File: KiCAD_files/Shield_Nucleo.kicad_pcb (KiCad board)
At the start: 4 copper layers, 90 x 100 mm, 62 parts, among them J1 Shield_nucleo_stage_outline, J2 RJ45_LED_Shielded, J3 RJ45_LED_Shielded, J4 Conn_01x02_Male, J5 Conn_01x04_Male, U1 NUCLEO-F401RE, U2 AT25xxx, U3 TCAN334GDR

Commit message: WIP: nearly finished composant placement
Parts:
- removed J1: Shield_nucleo_stage_outline, Footprints:Shield_nucleo_outline
- added C10: 100nF, Capacitor_SMD:C_0805_2012Metric, F.Cu at (61.5, 84.9)
- added C11: 100nF, Capacitor_SMD:C_0805_2012Metric, F.Cu at (119.4, 51.1)
- added C12: 1µF, Capacitor_SMD:C_0805_2012Metric, F.Cu at (94.9, 82.4)
- added C13: 100nF, Capacitor_SMD:C_0805_2012Metric, F.Cu at (118.3, 44.4)
- added C14: 10nF, Capacitor_SMD:C_0805_2012Metric, F.Cu at (91.1, 80.5)
- added C17: 33pF, Capacitor_SMD:C_0805_2012Metric, F.Cu at (122.5, 57.4)
- added C18: 33pF, Capacitor_SMD:C_0805_2012Metric, F.Cu at (122.8, 50.2)
- added C20: 100nF, Capacitor_SMD:C_0805_2012Metric, F.Cu at (121.2, 47.4)
- added C21: 100nF, Capacitor_SMD:C_0805_2012Metric, F.Cu at (106.2, 53.8)
- added C22: 100nF, Capacitor_SMD:C_0805_2012Metric, F.Cu at (108.2, 47.2)
- added C23: 1uF, Capacitor_SMD:C_0805_2012Metric, F.Cu at (104.4, 53.8)
- added C24: 10uF, Capacitor_SMD:C_1210_3225Metric, F.Cu at (104.4, 46.5)
- added C25: 100nF, Capacitor_SMD:C_0805_2012Metric, F.Cu at (71.3, 50.4)
- added C26: 100nF, Capacitor_SMD:C_0805_2012Metric, F.Cu at (70.3, 43.6)
- added C27: 33pF, Capacitor_SMD:C_0805_2012Metric, F.Cu at (74.6, 55.8)
- added C28: 33pF, Capacitor_SMD:C_0805_2012Metric, F.Cu at (74.6, 50.4)
- added C3: 12pF, Capacitor_SMD:C_0805_2012Metric, F.Cu at (70.3, 80.3)
- added C30: 100nF, Capacitor_SMD:C_0805_2012Metric, F.Cu at (73.1, 46.7)
- added C31: 100nF, Capacitor_SMD:C_0805_2012Metric, F.Cu at (59.1, 52.8)
- added C32: 100nF, Capacitor_SMD:C_0805_2012Metric, F.Cu at (59.7, 46.6)
- added C33: 1uF, Capacitor_SMD:C_0805_2012Metric, F.Cu at (57.3, 52.8)
- added C34: 10uF, Capacitor_SMD:C_1210_3225Metric, F.Cu at (55.7, 46.1)
- added C4: 12pF, Capacitor_SMD:C_0805_2012Metric, F.Cu at (74.8, 85.2)
- added C5: 100nF, Capacitor_SMD:C_0805_2012Metric, F.Cu at (60.3, 80.3)
- added C6: 4,7uF, Capacitor_SMD:C_0805_2012Metric, F.Cu at (-3.77, 84.7)
- added C7: 100nF, Capacitor_SMD:C_0805_2012Metric, F.Cu at (73.2, 71.6)
- added C8: 100nF, Capacitor_SMD:C_0805_2012Metric, F.Cu at (86.0, 67.2)
- added C9: 100nF, Capacitor_SMD:C_0805_2012Metric, F.Cu at (92.9, 78.6)
- added D10: STTH4R02U, Diode_SMD:D_SMB, F.Cu at (105.4, 59.2)
- added D11: STTH4R02U, Diode_SMD:D_SMB, F.Cu at (58.3, 58.1)
- added D3: 3.3V, Diode_SMD:D_SOD-123, F.Cu at (80.0, 94.4)
- added D4: 3.3V, Diode_SMD:D_SOD-123, F.Cu at (73.7, 99.1)
- added D5: 3.3V, Diode_SMD:D_SOD-123, F.Cu at (90.2, 94.4)
- added D6: 3.3V, Diode_SMD:D_SOD-123, F.Cu at (94.0, 99.1)
- added D7: 3.3V, Diode_SMD:D_SOD-123, F.Cu at (79.6, 104.1)
- added D8: 3.3V, Diode_SMD:D_SOD-123, F.Cu at (90.2, 105.4)
- added D9: 3.3V, Diode_SMD:D_SOD-123, F.Cu at (69.5, 105.4)
- added FB1: Ferrite_Bead_Small, Resistor_SMD:R_0805_2012Metric, F.Cu at (94.2, 77.3)
- added PS1: IA0505S, Converter_DCDC:Converter_DCDC_muRata_CRE1xxxxxx3C_THT, F.Cu at (105.5, 115.4)
- added PS2: IA0512S, Converter_DCDC:Converter_DCDC_muRata_CRE1xxxxxx3C_THT, F.Cu at (97.8, 115.4)
- added PS4: PQDE6W-Q110-S5-D, Footprints:PQDE6W-Q110-S5-D, F.Cu at (124.5, 113.2)
- added R14: 51, Resistor_SMD:R_0805_2012Metric, F.Cu at (122.6, 52.6)
- added R15: 20k, Resistor_SMD:R_0805_2012Metric, F.Cu at (119.4, 47.3)
- added R16: 2.2, Resistor_SMD:R_0805_2012Metric, F.Cu at (103.2, 63.0)
- added R17: 51, Resistor_SMD:R_0805_2012Metric, F.Cu at (74.6, 54.0)
- added R18: 51, Resistor_SMD:R_0805_2012Metric, F.Cu at (74.6, 52.2)
- added R19: 20k, Resistor_SMD:R_0805_2012Metric, F.Cu at (71.3, 46.7)
- added R20: 2.2, Resistor_SMD:R_0805_2012Metric, F.Cu at (60.7, 61.9)
- added R21: 51, Resistor_SMD:R_0805_2012Metric, F.Cu at (82.2, 111.8)
- added R22: 1k, Resistor_SMD:R_0805_2012Metric, F.Cu at (82.2, 119.4)
- added R23: 220, Resistor_SMD:R_0805_2012Metric, F.Cu at (75.8, 81.2)
- added TP16: TestPoint, TestPoint:TestPoint_Pad_D1.5mm, B.Cu at (134.7, 107.4)
- added TP31: TestPoint, TestPoint:TestPoint_Pad_D1.5mm, B.Cu at (50.0, 48.3)
- added TP34: TestPoint, TestPoint:TestPoint_Pad_D1.5mm, B.Cu at (94.2, 45.3)
- added TP35: TestPoint, TestPoint:TestPoint_Pad_D1.5mm, B.Cu at (94.2, 58.4)
- added TP36: TestPoint, TestPoint:TestPoint_Pad_D1.5mm, B.Cu at (94.2, 47.9)
- added TP37: TestPoint, TestPoint:TestPoint_Pad_D1.5mm, B.Cu at (83.8, 121.9)
- added TP38: TestPoint, TestPoint:TestPoint_Pad_D1.5mm, B.Cu at (81.1, 103.9)
- added TP39: TestPoint, TestPoint:TestPoint_Pad_D1.5mm, B.Cu at (89.3, 105.7)
- added TP40: TestPoint, TestPoint:TestPoint_Pad_D1.5mm, B.Cu at (79.4, 95.9)
- added TP41: TestPoint, TestPoint:TestPoint_Pad_D1.5mm, B.Cu at (89.7, 95.8)
- added TP42: TestPoint, TestPoint:TestPoint_Pad_D1.5mm, B.Cu at (92.2, 98.4)
- added TP43: TestPoint, TestPoint:TestPoint_Pad_D1.5mm, B.Cu at (50.0, 61.0)
- added TP44: TestPoint, TestPoint:TestPoint_Pad_D1.5mm, B.Cu at (94.2, 61.0)
- added TP45: TestPoint, TestPoint:TestPoint_Pad_D1.5mm, B.Cu at (81.3, 121.9)
- added U4: AP1117-33, Package_TO_SOT_SMD:SOT-223-3_TabPin2, F.Cu at (111.0, 76.2)
- added U5: UCC21222DR, Package_SO:SOIC-16_4.55x10.3mm_P1.27mm, F.Cu at (114.0, 50.2)
- added U6: UCC21222DR, Package_SO:SOIC-16_4.55x10.3mm_P1.27mm, F.Cu at (65.7, 49.6)
- added U7: SFH617A-2X009T, Package_DIP:SMDIP-4_W7.62mm, F.Cu at (85.8, 115.8)
- added Y1: NX3225SA-16.000000MHZ-T1, Crystal:Crystal_SMD_3225-4Pin_3.2x2.5mm, F.Cu at (72.4, 82.8)
- BT1, C1, C2, D1, D2, F1, F2, JP1, R1, R2, R4, R6, R8, U2, U3: moved to F.Cu
- R3, R5, R7: value 39k -> 20k; moved to F.Cu
- R9: value 39k -> 51; moved to F.Cu
- TP1, TP10, TP11, TP12, TP13, TP14, TP15, TP17, TP18, TP19, TP2, TP20, TP3, TP32, TP33, TP4, TP5, TP6, TP7, TP8, TP9: footprint TestPoint:TestPoint_THTPad_D2.0mm_Drill1.0mm -> TestPoint:TestPoint_Pad_D1.5mm
- TP21, TP22, TP23, TP24, TP25, TP26, TP27, TP28, TP29, TP30: footprint TestPoint:TestPoint_THTPad_D2.0mm_Drill1.0mm -> TestPoint:TestPoint_Pad_D1.5mm; moved to B.Cu
- U1: value NUCLEO-F401RE -> STM32G474RE; footprint Footprints:ST_NUCLEO-G474 -> Package_QFP:LQFP-64_10x10mm_P0.5mm
- moved J2 129.7 mm to (187.7, 27.4), turned to 180 degrees
- moved R11 129.5 mm to (192.8, 33.2), turned to 270 degrees
- moved R10 112.7 mm to (181.4, 33.1), turned to 270 degrees
- moved J3 104.5 mm to (167.6, 27.4), turned to 180 degrees
- moved C2 102.9 mm to (182.5, 46.0), turned to 90 degrees
- moved U3 101.4 mm to (187.1, 46.0)
- moved R13 101.2 mm to (172.7, 33.0), turned to 270 degrees
- moved JP1 100.6 mm to (192.2, 44.4), turned to 270 degrees
- moved R1 97.5 mm to (192.2, 47.1), turned to 270 degrees
- moved BT1 90.7 mm to (50.8, 111.9), turned to 90 degrees
- moved R12 88.8 mm to (161.3, 33.1), turned to 270 degrees
- moved J4 84.1 mm to (152.2, 109.6)
- moved F1 82.6 mm to (175.0, 46.2)
- moved J5 81.8 mm to (152.2, 115.4)
- moved TP22 80.2 mm to (134.7, 118.8), turned to 180 degrees
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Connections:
- R2 pad 1: Net-(J1-Pad9) -> /I1_low_mcu
- R2 pad 2: /I1_low -> /I1_low_op
- R3 pad 1: /I1_low -> /V1_low_mcu
- R3 pad 2: GNDD -> /V1_low_op
- R4 pad 1: Net-(J1-Pad10) -> /I1_low_mcu
- R4 pad 2: /I2_low -> /I2_low_op
- R5 pad 1: /I2_low -> /V2_low_mcu
- R5 pad 2: GNDD -> /V2_low_op
- R6 pad 1: Net-(J1-Pad11) -> /I_high_mcu
- R6 pad 2: /I_high -> /I_high_op
- R7 pad 1: /I_high -> /V_high_mcu
- R7 pad 2: GNDD -> /V_high_op
- R8 pad 1: Net-(J1-Pad12) -> /Temp
- R9 pad 1: /Temp -> /HRTIM1_CHA1
- R9 pad 2: GNDD -> Net-(C17-Pad2)
- TP21 pad 1: /V1_low_P -> /V1_low_op
- TP22 pad 1: /V1_low_N -> GNDREF
- TP23 pad 1: /V2_low_P -> /V2_low_op
- TP24 pad 1: /V2_low_N -> /PWM_H1
- TP25 pad 1: /V_high_P -> /V_high_op
- TP26 pad 1: /V_high_N -> /PWM_L1
- TP27 pad 1: /I1_low -> /I1_low_op
- TP28 pad 1: /I2_low -> /I2_low_op
- TP29 pad 1: /I_high -> /I_high_op
- TP30 pad 1: /Temp -> GNDD
- U1 pad 1: (no net) -> +BATT
- U1 pad 2: (no net) -> Net-(U1-Pad2)
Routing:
- net +BATT: track 221.5 -> 0.00 mm
- net +3V3: track 204.9 -> 26.2 mm, vias 3 -> 1
- net /I2_low: track 165.6 -> 0.00 mm, vias 1 -> 0
- net /I_high: track 162.7 -> 0.00 mm, vias 1 -> 0
- net /HRTIM1_CHB1: track 158.1 -> 0.25 mm
- net /V1_low_N: track 144.7 -> 0.00 mm, vias 1 -> 0
- net /SPI3_MISO: track 139.3 -> 0.00 mm
- net /V1_low_P: track 138.3 -> 0.00 mm, vias 1 -> 0
- net /SPI3_MOSI: track 133.9 -> 0.00 mm
- net /I1_low: track 129.2 -> 0.00 mm, vias 2 -> 0
- net /HRTIM1_CHB2: track 127.3 -> 0.00 mm, vias 1 -> 0
- net /SPI3_CS2: track 122.2 -> 0.00 mm, vias 2 -> 0
- net /GND_CAN: track 112.7 -> 0.00 mm, vias 2 -> 0
- net /USART1_TX: track 106.2 -> 0.00 mm, vias 2 -> 0
- net /SPI3_SCK: track 103.4 -> 0.00 mm
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- removed copper zone on In2.Cu, net GNDD
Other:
- board size 90 x 100 mm -> 100 x 100 mm
- board text added: "V1H"
- board text added: "V1L"
- board text added: "V2L"
- board text removed: "V1HN"
- board text removed: "V1HP"
- board text removed: "V1LN"
- board text removed: "V1LP"
- board text removed: "V2LN"
- board text removed: "V2LP"

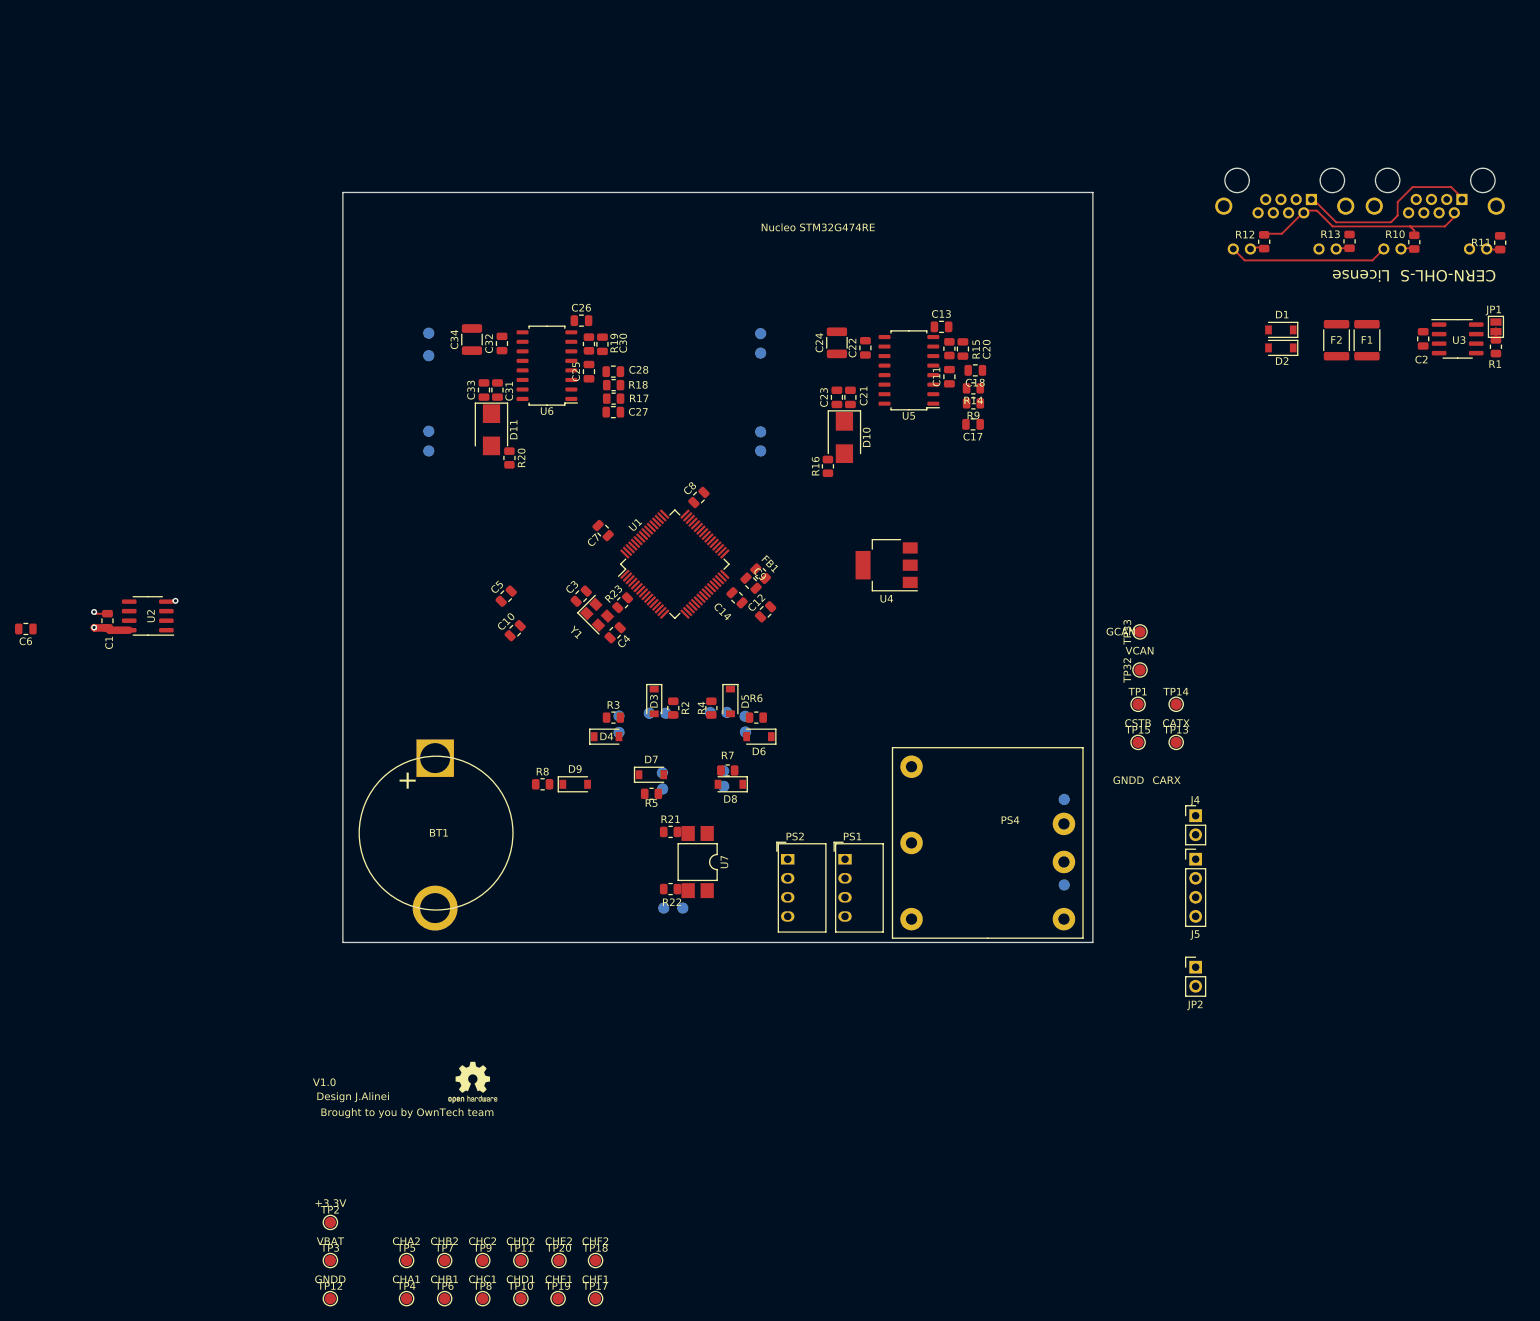
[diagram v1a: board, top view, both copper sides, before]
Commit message: WIP: Added power 3D footprint, placed the feeder, the MCU Remapping differential to single ended to be done and ready to route
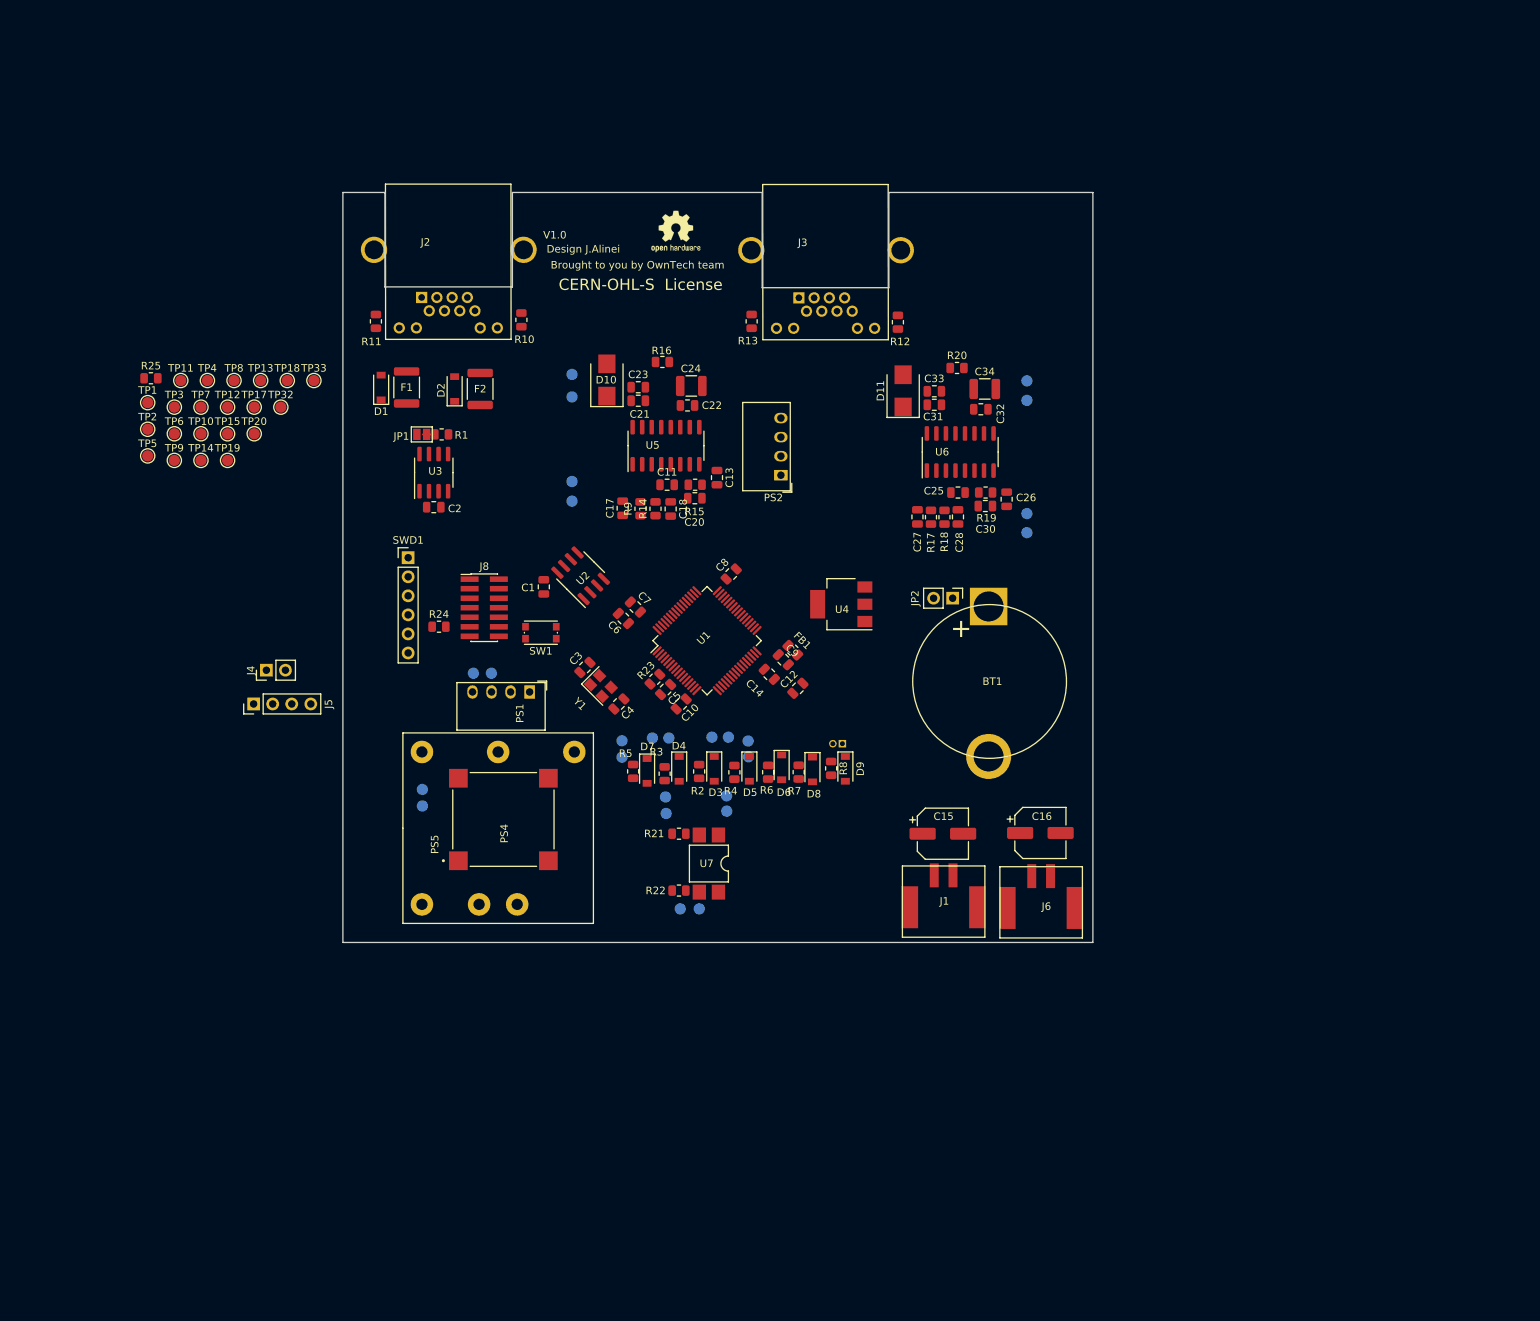
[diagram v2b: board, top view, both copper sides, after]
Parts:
- added 3D1: 3D_Footprint, Footprints:3D_Footprint_Power, F.Cu at (38.5, 26.5)
- added C15: CP1_Small, Capacitor_SMD:CP_Elec_6.3x7.7, F.Cu at (118.5, 112.0)
- added C16: CP1_Small, Capacitor_SMD:CP_Elec_6.3x7.7, F.Cu at (131.5, 111.9)
- added J1: Conn_01x02, Footprints:PTSM-0,5-2-HH0-SMD, F.Cu at (118.6, 121.8)
- added J6: Conn_01x02, Footprints:PTSM-0,5-2-HH0-SMD, F.Cu at (131.6, 121.9)
- added J8: Conn_02x07_Odd_Even, Connector_PinHeader_1.27mm:PinHeader_2x07_P1.27mm_Vertical_SMD, F.Cu at (57.4, 81.9)
- added PS5: VXO78xxx, Footprints:CONV_VXO78012-500-M, F.Cu at (59.9, 110.1)
- added R24: 100, Resistor_SMD:R_0805_2012Metric, F.Cu at (51.3, 84.4)
- added R25: 20k, Resistor_SMD:R_0805_2012Metric, F.Cu at (12.9, 51.3)
- added SW1: SW_Push, Button_Switch_SMD:SW_Push_1P1T_NO_CK_KMR2, F.Cu at (64.9, 85.2)
- added SWD1: Conn_01x06_Female, Connector_PinHeader_2.54mm:PinHeader_1x06_P2.54mm_Vertical, F.Cu at (47.2, 75.2)
- added TH1: NXFT15XH103FA2B100, Connector_PinHeader_1.27mm:PinHeader_1x02_P1.27mm_Horizontal, B.Cu at (105.1, 100.0)
- added TP46: TestPoint, TestPoint:TestPoint_Pad_D1.5mm, B.Cu at (58.3, 90.6)
- added TP47: TestPoint, TestPoint:TestPoint_Pad_D1.5mm, B.Cu at (55.9, 90.6)
- J2, J3: footprint Connector_RJ:RJ45_Amphenol_RJHSE538X -> Footprints:ethernet_RJE721881411; moved to F.Cu
- U5, U6: footprint Package_SO:SOIC-16_4.55x10.3mm_P1.27mm -> Footprints:SOIC-16_3.9x9.9mm_P1.27mm
- moved R11 150.3 mm to (42.9, 43.7)
- moved JP1 143.9 mm to (49.0, 58.8), turned to 0 degrees
- moved R1 141.1 mm to (51.7, 58.8), turned to 0 degrees
- moved J2 139.3 mm to (49.0, 40.5), turned to 0 degrees
- moved TP1 138.0 mm to (12.5, 54.5)
- moved U3 137.7 mm to (50.6, 63.9), turned to 90 degrees
- moved TP14 134.0 mm to (19.6, 62.2)
- moved C2 133.8 mm to (50.6, 68.5), turned to 180 degrees
- moved TP13 131.3 mm to (27.5, 51.6)
- moved F1 128.2 mm to (47.0, 52.5), turned to 90 degrees
- moved TP15 128.2 mm to (23.1, 58.7)
- moved J5 127.3 mm to (26.6, 94.7), turned to 90 degrees
- moved TP17 127.3 mm to (26.7, 55.1)
- moved TP8 126.8 mm to (24.0, 51.6)
- moved TP11 125.8 mm to (16.9, 51.6)
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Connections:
- net Net-(C5-Pad1) renamed /NRST
- U1 pad 14: Net-(U1-Pad14) -> /STLINK_RX
- U1 pad 17: Net-(U1-Pad17) -> /STLINK_TX
- U1 pad 49: Net-(U1-Pad49) -> /SWDIO
- U1 pad 50: Net-(U1-Pad50) -> /SWCLK
- U1 pad 56: Net-(U1-Pad56) -> /SWO
- U1 pad 60: Net-(U1-Pad60) -> /USART1_RX
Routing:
- net /CAN_L: track 30.1 -> 0.00 mm
- net +3V3: track 26.2 -> 0.00 mm, vias 1 -> 0
- net /CAN_H: track 25.1 -> 0.00 mm
- net GNDD: track 3.14 -> 0.00 mm, vias 2 -> 0
- net Net-(J3-Pad9): track 2.30 -> 0.00 mm
- net Net-(J3-Pad11): track 2.07 -> 0.00 mm
- net Net-(J2-Pad9): track 1.83 -> 0.00 mm
- net Net-(J2-Pad11): track 1.82 -> 0.00 mm
- net /EEPROM_HOLD: track 0.51 -> 0.00 mm
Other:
- outline, holes or cut-outs redrawn
- board text removed: "+3.3V"
- board text removed: "CARX"
- board text removed: "CATX"
- board text removed: "CHA1"
- board text removed: "CHA2"
- board text removed: "CHB1"
- board text removed: "CHB2"
- board text removed: "CHC1"
- board text removed: "CHC2"
- board text removed: "CHD1"
- board text removed: "CHD2"
- board text removed: "CHE1"
- board text removed: "CHE2"
- board text removed: "CHF1"
- board text removed: "CHF2"
- board text removed: "CSTB"
- board text removed: "GCAN"
- board text removed: "GNDD"
- board text removed: "Nucleo STM32G474RE"
- board text removed: "TMP"
- board text removed: "VBAT"
- board text removed: "VCAN"
